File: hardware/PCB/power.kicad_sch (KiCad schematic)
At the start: 68 parts

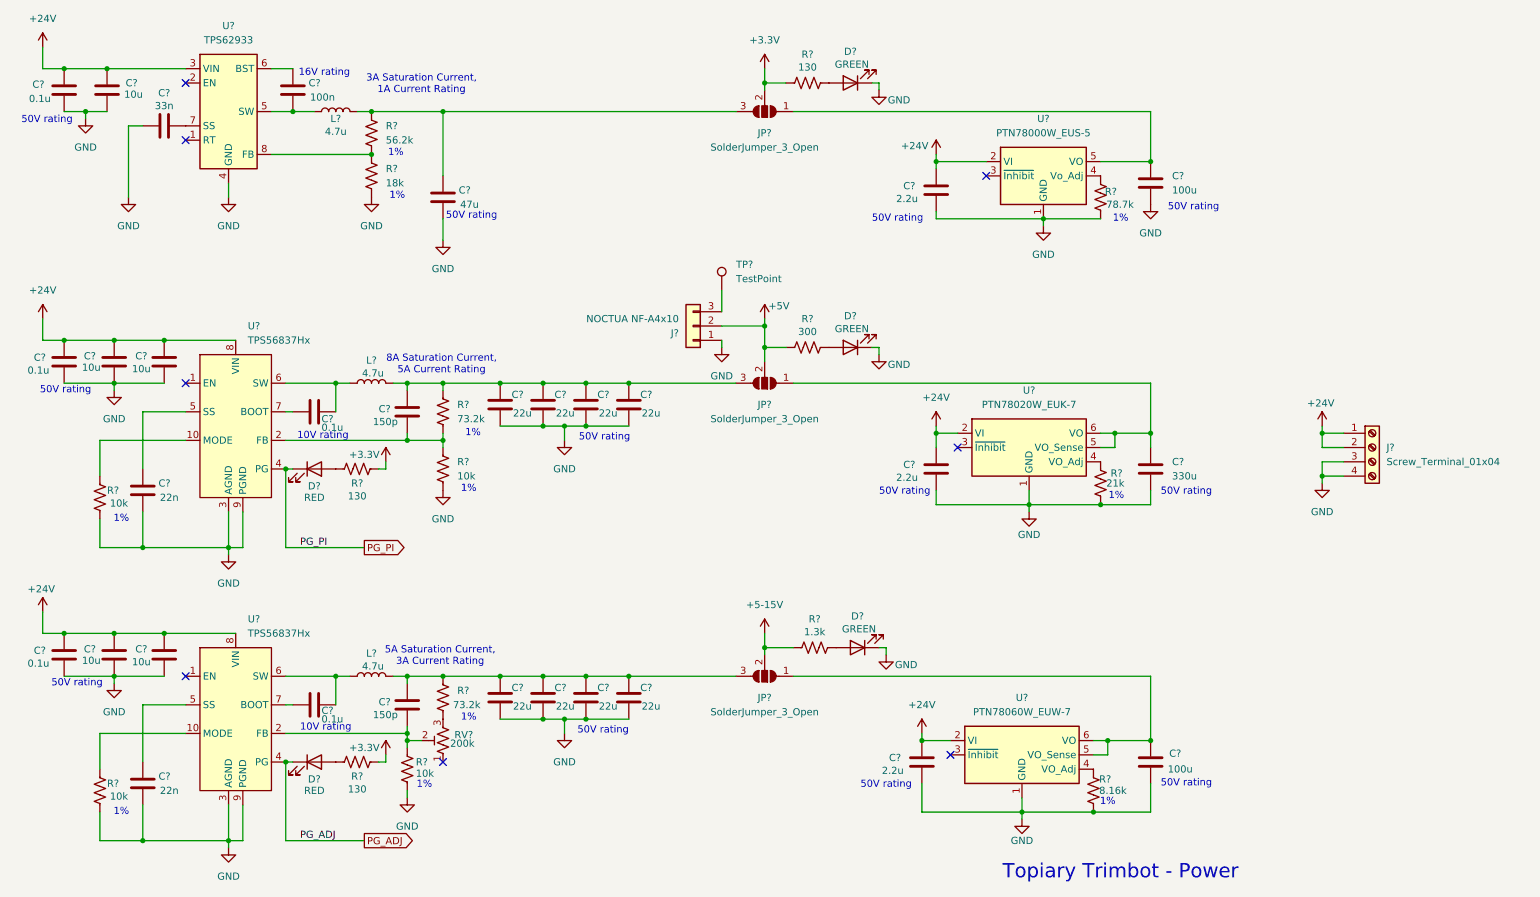
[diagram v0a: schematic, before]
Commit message: Schematic - 24V fan & Driver Test Points
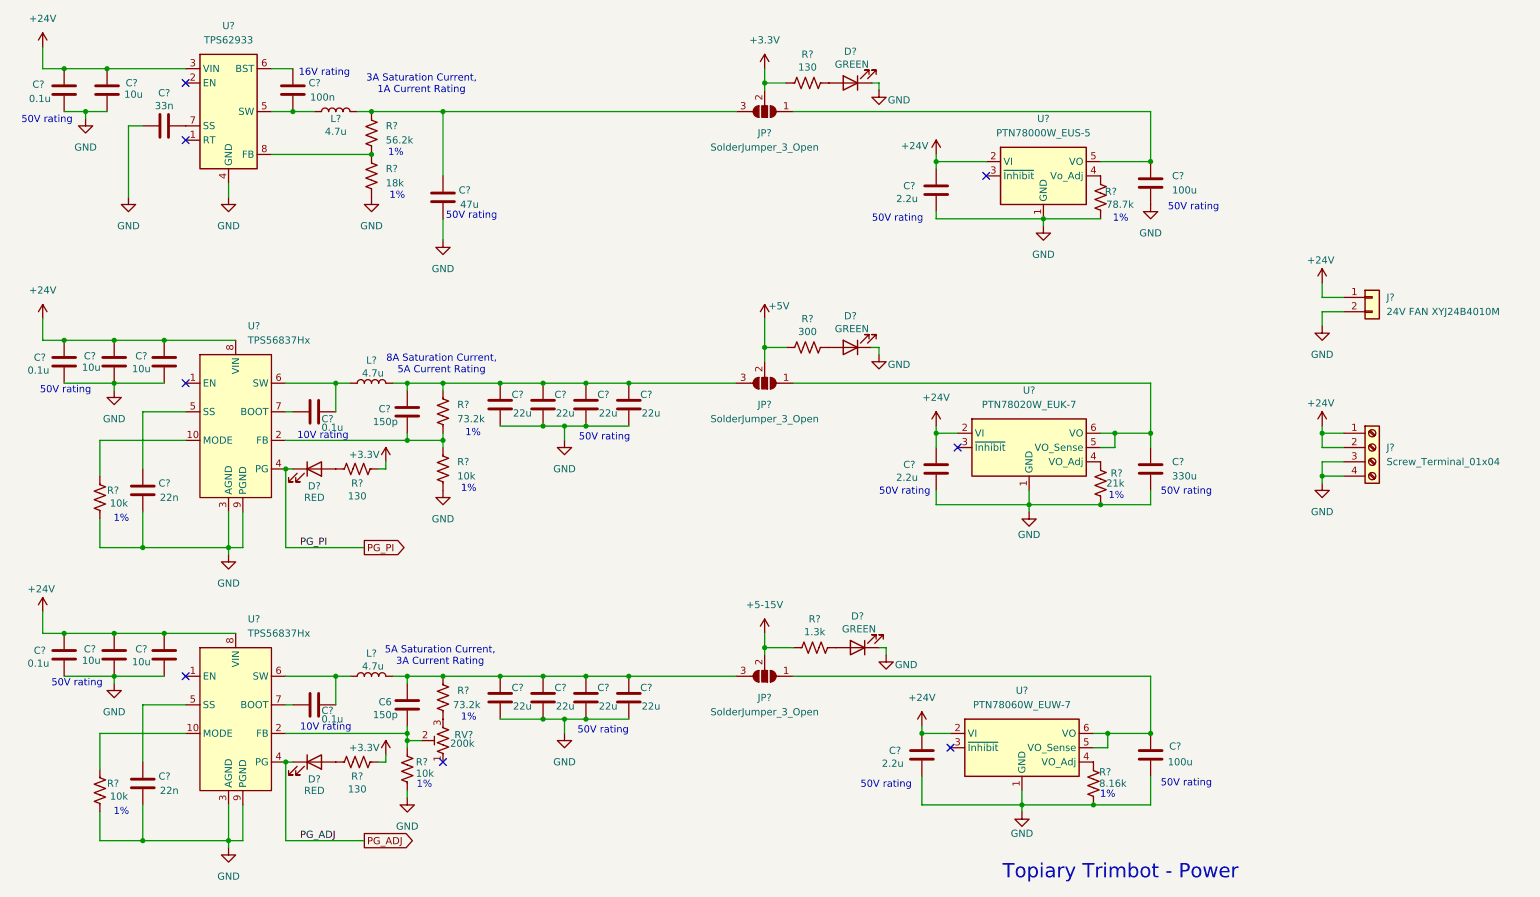
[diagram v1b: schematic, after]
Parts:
- removed J?: NOCTUA NF-A4x10, symbol Connector_Generic:Conn_01x03
- removed TP?: TestPoint, symbol Connector:TestPoint
- added J?: 24V FAN XYJ24B4010M, symbol Connector_Generic:Conn_01x02
- gave numbers to parts that had none: 1
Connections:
- net +24V: now also J?.1 (Pin_1)
- net GND: now also J?.2 (Pin_2)
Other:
- moved on the sheet: C?, R?, U?

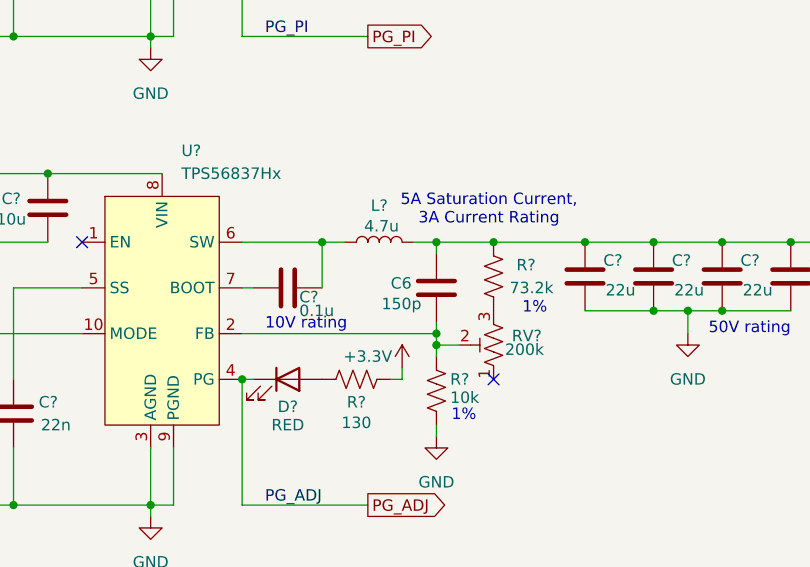
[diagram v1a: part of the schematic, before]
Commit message: Schematic - Motor Control Error
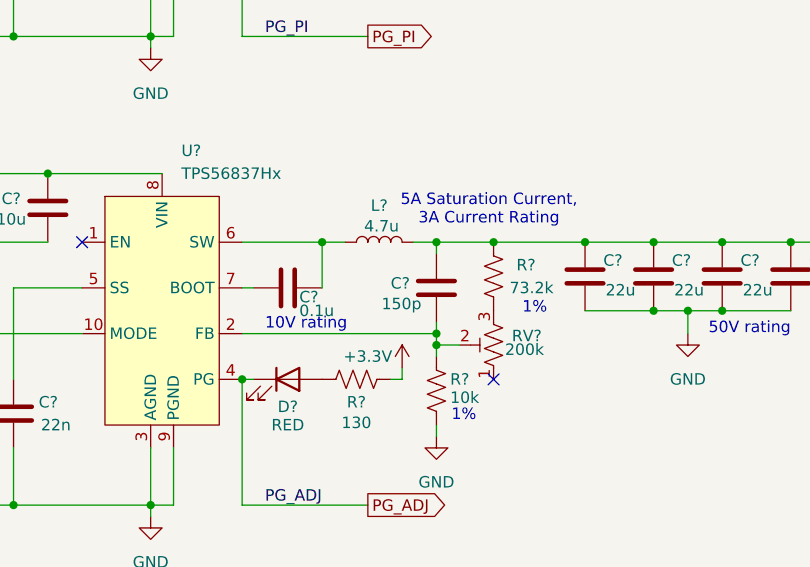
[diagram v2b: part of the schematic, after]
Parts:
- renumbered C6 to C?
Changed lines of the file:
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@@
 		(dnp no)
 		(fields_autoplaced yes)
-		(property "Reference" "#PWR028"
+		(property "Reference" "#PWR?"
 			(at 90.17 109.22 0)
 			(effects
@@
 		(on_board yes)
 		(dnp no)
-		(property "Reference" "#PWR033"
+		(property "Reference" "#PWR?"
 			(at 168.91 138.43 0)
 			(effects
@@
 		(dnp no)
 		(fields_autoplaced yes)
-		(property "Reference" "#PWR016"
+		(property "Reference" "#PWR?"
 			(at 177.8 95.25 0)
 			(effects
@@
 		(on_board yes)
 		(dnp no)
-		(property "Reference" "#PWR017"
+		(property "Reference" "#PWR?"
 			(at 194.31 113.03 0)
 			(effects
@@
 		(dnp no)
 		(fields_autoplaced yes)
-		(property "Reference" "#PWR012"
+		(property "Reference" "#PWR?"
 			(at 83.82 163.83 0)
 			(effects
@@
 		(on_board yes)
 		(dnp no)
-		(property "Reference" "#PWR06"
+		(property "Reference" "#PWR?"
 			(at 90.17 64.77 0)
 			(effects
@@
 		(dnp no)
 		(fields_autoplaced yes)
-		(property "Reference" "#PWR05"
+		(property "Reference" "#PWR?"
 			(at 77.47 57.15 0)
 			(effects
@@
 		(on_board yes)
 		(dnp no)
-		(property "Reference" "#PWR031"
+		(property "Reference" "#PWR?"
 			(at 167.64 38.1 0)
 			(effects
@@
 		(dnp no)
 		(fields_autoplaced yes)
-		(property "Reference" "#PWR02"
+		(property "Reference" "#PWR?"
 			(at 246.38 107.95 0)
 			(effects
@@
 		(dnp no)
 		(fields_autoplaced yes)
-		(property "Reference" "#PWR08"
+		(property "Reference" "#PWR?"
 			(at 31.75 143.51 0)
 			(effects
@@
 		(dnp no)
 		(fields_autoplaced yes)
-		(property "Reference" "#PWR026"
+		(property "Reference" "#PWR?"
 			(at 52.07 120.65 0)
 			(effects
@@
 		(dnp no)
 		(fields_autoplaced yes)
-		(property "Reference" "#PWR024"
+		(property "Reference" "#PWR?"
 			(at 31.75 91.44 0)
 			(effects
@@
 		(dnp no)
 		(fields_autoplaced yes)
-		(property "Reference" "#PWR025"
+		(property "Reference" "#PWR?"
 			(at 19.05 76.2 0)
 			(effects
@@
 		(on_board yes)
 		(dnp no)
-		(property "Reference" "#PWR022"
+		(property "Reference" "#PWR?"
 			(at 193.04 166.37 0)
 			(effects
@@
 		(dnp no)
 		(fields_autoplaced yes)
-		(property "Reference" "#PWR030"
+		(property "Reference" "#PWR?"
 			(at 111.76 100.33 0)
 			(effects
@@
 		(on_board yes)
 		(dnp no)
-		(property "Reference" "#PWR032"
+		(property "Reference" "#PWR?"
 			(at 167.64 85.09 0)
 			(effects
@@
 		(dnp no)
 		(fields_autoplaced yes)
-		(property "Reference" "#PWR013"
+		(property "Reference" "#PWR?"
 			(at 111.76 152.4 0)
 			(effects
@@
 		(dnp no)
 		(fields_autoplaced yes)
-		(property "Reference" "#PWR021"
+		(property "Reference" "#PWR?"
 			(at 175.26 148.59 0)
 			(effects
@@
 		(on_board yes)
 		(dnp no)
-		(property "Reference" "#PWR?"
+		(property "Reference" "#PWR080"
 			(at 246.38 69.85 0)
 			(effects
@@
 		(dnp no)
 		(fields_autoplaced yes)
-		(property "Reference" "#PWR023"
+		(property "Reference" "#PWR?"
 			(at 215.9 58.42 0)
 			(effects
@@
 		(on_board yes)
 		(dnp no)
-		(property "Reference" "#PWR09"
+		(property "Reference" "#PWR?"
 			(at 246.38 95.25 0)
 			(effects
@@
 		(on_board yes)
 		(dnp no)
-		(property "Reference" "#PWR027"
+		(property "Reference" "#PWR?"
 			(at 80.01 101.6 0)
 			(effects
@@
 		(dnp no)
 		(fields_autoplaced yes)
-		(property "Reference" "#PWR04"
+		(property "Reference" "#PWR?"
 			(at 34.29 57.15 0)
 			(effects
@@
 		(on_board yes)
 		(dnp no)
-		(property "Reference" "#PWR029"
+		(property "Reference" "#PWR?"
 			(at 147.32 76.2 0)
 			(effects
@@
 		(on_board yes)
 		(dnp no)
-		(property "Reference" "C6"
+		(property "Reference" "C?"
 			(at 78.74 140.462 0)
 			(effects
@@
 		(on_board yes)
 		(dnp no)
-		(property "Reference" "#PWR07"
+		(property "Reference" "#PWR?"
 			(at 19.05 128.27 0)
 			(effects
@@
 		(dnp no)
 		(fields_autoplaced yes)
-		(property "Reference" "#PWR01"
+		(property "Reference" "#PWR?"
 			(at 52.07 57.15 0)
 			(effects
@@
 		(dnp no)
 		(fields_autoplaced yes)
-		(property "Reference" "#PWR010"
+		(property "Reference" "#PWR?"
 			(at 52.07 172.72 0)
 			(effects
@@
 		(dnp no)
 		(fields_autoplaced yes)
-		(property "Reference" "#PWR?"
+		(property "Reference" "#PWR081"
 			(at 246.38 80.01 0)
 			(effects
@@
 		(dnp no)
 		(fields_autoplaced yes)
-		(property "Reference" "#PWR014"
+		(property "Reference" "#PWR?"
 			(at 19.05 27.94 0)
 			(effects
@@
 		(dnp no)
 		(fields_autoplaced yes)
-		(property "Reference" "#PWR015"
+		(property "Reference" "#PWR?"
 			(at 143.256 127.254 0)
 			(effects
@@
 		(dnp no)
 		(fields_autoplaced yes)
-		(property "Reference" "#PWR03"
+		(property "Reference" "#PWR?"
 			(at 26.67 43.18 0)
 			(effects
@@
 		(dnp no)
 		(fields_autoplaced yes)
-		(property "Reference" "#PWR018"
+		(property "Reference" "#PWR?"
 			(at 147.32 31.75 0)
 			(effects
@@
 		(on_board yes)
 		(dnp no)
-		(property "Reference" "#PWR011"
+		(property "Reference" "#PWR?"
 			(at 80.01 153.67 0)
 			(effects
@@
 		(on_board yes)
 		(dnp no)
-		(property "Reference" "#PWR020"
+		(property "Reference" "#PWR?"
 			(at 177.8 46.99 0)
 			(effects
@@
 		(dnp no)
 		(fields_autoplaced yes)
-		(property "Reference" "#PWR019"
+		(property "Reference" "#PWR?"
 			(at 196.85 62.23 0)
 			(effects

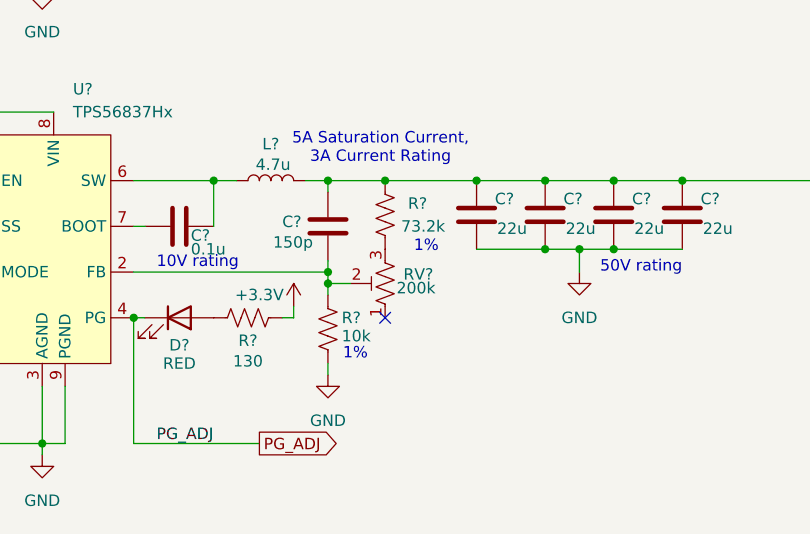
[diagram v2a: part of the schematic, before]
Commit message: Footprint edits
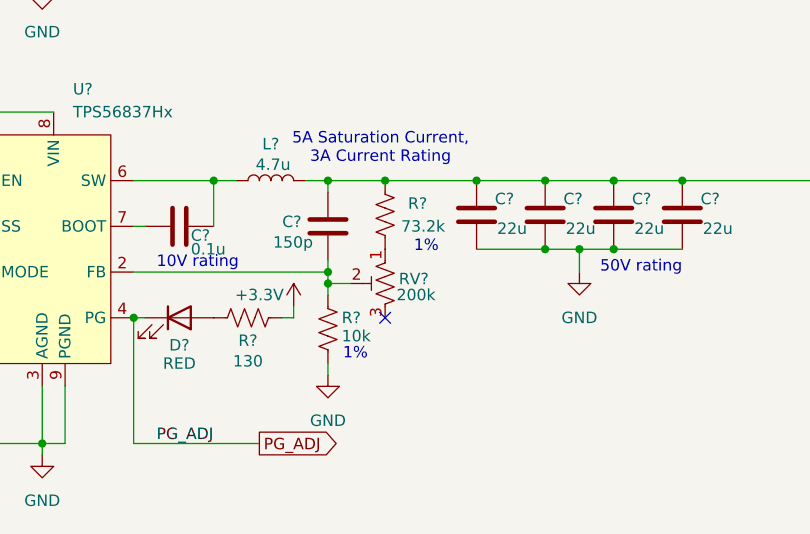
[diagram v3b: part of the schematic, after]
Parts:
- RV?: MANUFACTURER (none) -> Bourns; Manufacturer_Part_Number (none) -> 3362P-1-204LF
- U? (x3): MANUFACTURER (none) -> Texas Instruments
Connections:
- net at RV?.1: now also R?.2
- net at RV?.3: no longer R?.2
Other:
- moved on the sheet: RV?
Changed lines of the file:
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@@
 			)
 		)
+		(property "MANUFACTURER" "Texas Instruments"
+			(at 194.31 95.25 0)
+			(effects
+				(font
+					(size 1.27 1.27)
+				)
+				(hide yes)
+			)
+		)
 		(pin "7"
 		)
@@
 	(symbol
 		(lib_id "Device:R_Potentiometer_Trim_US")
-		(at 90.17 147.32 180)
+		(at 90.17 147.32 0)
+		(mirror y)
 		(unit 1)
 		(exclude_from_sim no)
@@
 		(dnp no)
 		(property "Reference" "RV?"
-			(at 92.202 146.304 0)
+			(at 91.694 146.812 0)
 			(effects
 				(font
@@
 		)
 		(property "Value" "200k"
-			(at 91.44 147.828 0)
+			(at 91.44 148.59 0)
 			(effects
 				(font
@@
 			)
 		)
-		(property "Datasheet" "~"
+		(property "Datasheet" "https://www.bourns.com/docs/Product-Datasheets/3362.pdf"
 			(at 90.17 147.32 0)
 			(effects
@@
 			)
 		)
+		(property "MANUFACTURER" "Bourns"
+			(at 90.17 147.32 0)
+			(effects
+				(font
+					(size 1.27 1.27)
+				)
+				(hide yes)
+			)
+		)
+		(property "Manufacturer_Part_Number" "3362P-1-204LF"
+			(at 90.17 147.32 0)
+			(effects
+				(font
+					(size 1.27 1.27)
+				)
+				(hide yes)
+			)
+		)
 		(pin "3"
 		)
@@
 				)
 			)
-			(project ""
-				(path "/288cd01c-b1d5-44ca-91a2-b9192151afef"
-					(reference "RV?")
-					(unit 1)
-				)
-			)
 		)
 	)
@@
 			)
 		)
+		(property "MANUFACTURER" "Texas Instruments"
+			(at 196.85 46.99 0)
+			(effects
+				(font
+					(size 1.27 1.27)
+				)
+				(hide yes)
+			)
+		)
 		(pin "1"
 		)
@@
 			(at 193.04 148.59 0)
 			(effects
+				(font
+					(size 1.27 1.27)
+				)
+				(hide yes)
+			)
+		)
+		(property "MANUFACTURER" "Texas Instruments"
+			(at 193.04 148.59 0)
+			(effects

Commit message: Schematic - Power Footprints
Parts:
- D? (x5): footprint (none) -> LED_SMD:LED_0805_2012Metric
- J?: footprint (none) -> Connector_PinHeader_2.54mm:PinHeader_1x02_P2.54mm_Vertical
- J?: footprint (none) -> CustomFootprints:6DBL-04-006
- R? (x16): footprint (none) -> Resistor_SMD:R_0805_2012Metric
- RV?: footprint (none) -> CustomFootprints:3362P
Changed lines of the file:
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@@
 			)
 		)
-		(property "Footprint" ""
+		(property "Footprint" "LED_SMD:LED_0805_2012Metric"
 			(at 67.31 99.06 0)
 			(effects
@@
 			)
 		)
-		(property "Footprint" ""
+		(property "Footprint" "Resistor_SMD:R_0805_2012Metric"
 			(at 154.686 78.486 90)
 			(effects
@@
 			)
 		)
-		(property "Footprint" ""
+		(property "Footprint" "LED_SMD:LED_0805_2012Metric"
 			(at 162.56 30.48 0)
 			(effects
@@
 			)
 		)
-		(property "Footprint" ""
+		(property "Footprint" "Resistor_SMD:R_0805_2012Metric"
 			(at 74.676 100.076 90)
 			(effects
@@
 			)
 		)
-		(property "Footprint" ""
+		(property "Footprint" "LED_SMD:LED_0805_2012Metric"
 			(at 163.83 130.81 0)
 			(effects
@@
 			)
 		)
-		(property "Footprint" ""
+		(property "Footprint" "LED_SMD:LED_0805_2012Metric"
 			(at 67.31 151.13 0)
 			(effects
@@
 			)
 		)
-		(property "Footprint" ""
+		(property "Footprint" "LED_SMD:LED_0805_2012Metric"
 			(at 162.56 77.47 0)
 			(effects
@@
 			)
 		)
-		(property "Footprint" ""
+		(property "Footprint" "Resistor_SMD:R_0805_2012Metric"
 			(at 84.836 152.654 90)
 			(effects
@@
 			)
 		)
-		(property "Footprint" ""
+		(property "Footprint" "Resistor_SMD:R_0805_2012Metric"
 			(at 30.226 104.394 90)
 			(effects
@@
 			)
 		)
-		(property "Footprint" ""
+		(property "Footprint" "Resistor_SMD:R_0805_2012Metric"
 			(at 155.956 131.826 90)
 			(effects
@@
 			)
 		)
-		(property "Footprint" ""
+		(property "Footprint" "Resistor_SMD:R_0805_2012Metric"
 			(at 91.186 99.314 90)
 			(effects
@@
 			)
 		)
-		(property "Footprint" ""
+		(property "Footprint" "CustomFootprints:3362P"
 			(at 90.17 147.32 0)
 			(effects
@@
 			)
 		)
-		(property "Footprint" ""
+		(property "Footprint" "Resistor_SMD:R_0805_2012Metric"
 			(at 154.686 31.496 90)
 			(effects
@@
 			)
 		)
-		(property "Footprint" ""
+		(property "Footprint" "Resistor_SMD:R_0805_2012Metric"
 			(at 74.676 152.146 90)
 			(effects
@@
 			)
 		)
-		(property "Footprint" ""
+		(property "Footprint" "Connector_PinHeader_2.54mm:PinHeader_1x02_P2.54mm_Vertical"
 			(at 255.27 68.58 0)
 			(effects
@@
 			)
 		)
-		(property "Footprint" ""
+		(property "Footprint" "Resistor_SMD:R_0805_2012Metric"
 			(at 208.026 101.854 90)
 			(effects
@@
 			)
 		)
-		(property "Footprint" ""
+		(property "Footprint" "Resistor_SMD:R_0805_2012Metric"
 			(at 91.186 89.154 90)
 			(effects
@@
 			)
 		)
-		(property "Footprint" ""
+		(property "Footprint" "Resistor_SMD:R_0805_2012Metric"
 			(at 78.486 47.244 90)
 			(effects
@@
 			)
 		)
-		(property "Footprint" ""
+		(property "Footprint" "Resistor_SMD:R_0805_2012Metric"
 			(at 206.756 155.194 90)
 			(effects
@@
 			)
 		)
-		(property "Footprint" ""
+		(property "Footprint" "CustomFootprints:6DBL-04-006"
 			(at 255.27 95.25 0)
 			(effects
@@
 			)
 		)
-		(property "Footprint" ""
+		(property "Footprint" "Resistor_SMD:R_0805_2012Metric"
 			(at 91.186 139.954 90)
 			(effects
@@
 			)
 		)
-		(property "Footprint" ""
+		(property "Footprint" "Resistor_SMD:R_0805_2012Metric"
 			(at 208.026 51.054 90)
 			(effects
@@
 			)
 		)
-		(property "Footprint" ""
+		(property "Footprint" "Resistor_SMD:R_0805_2012Metric"
 			(at 30.226 156.464 90)
 			(effects
@@
 			)
 		)
-		(property "Footprint" ""
+		(property "Footprint" "Resistor_SMD:R_0805_2012Metric"
 			(at 78.486 39.624 90)
 			(effects
